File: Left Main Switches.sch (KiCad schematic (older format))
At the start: 80 parts

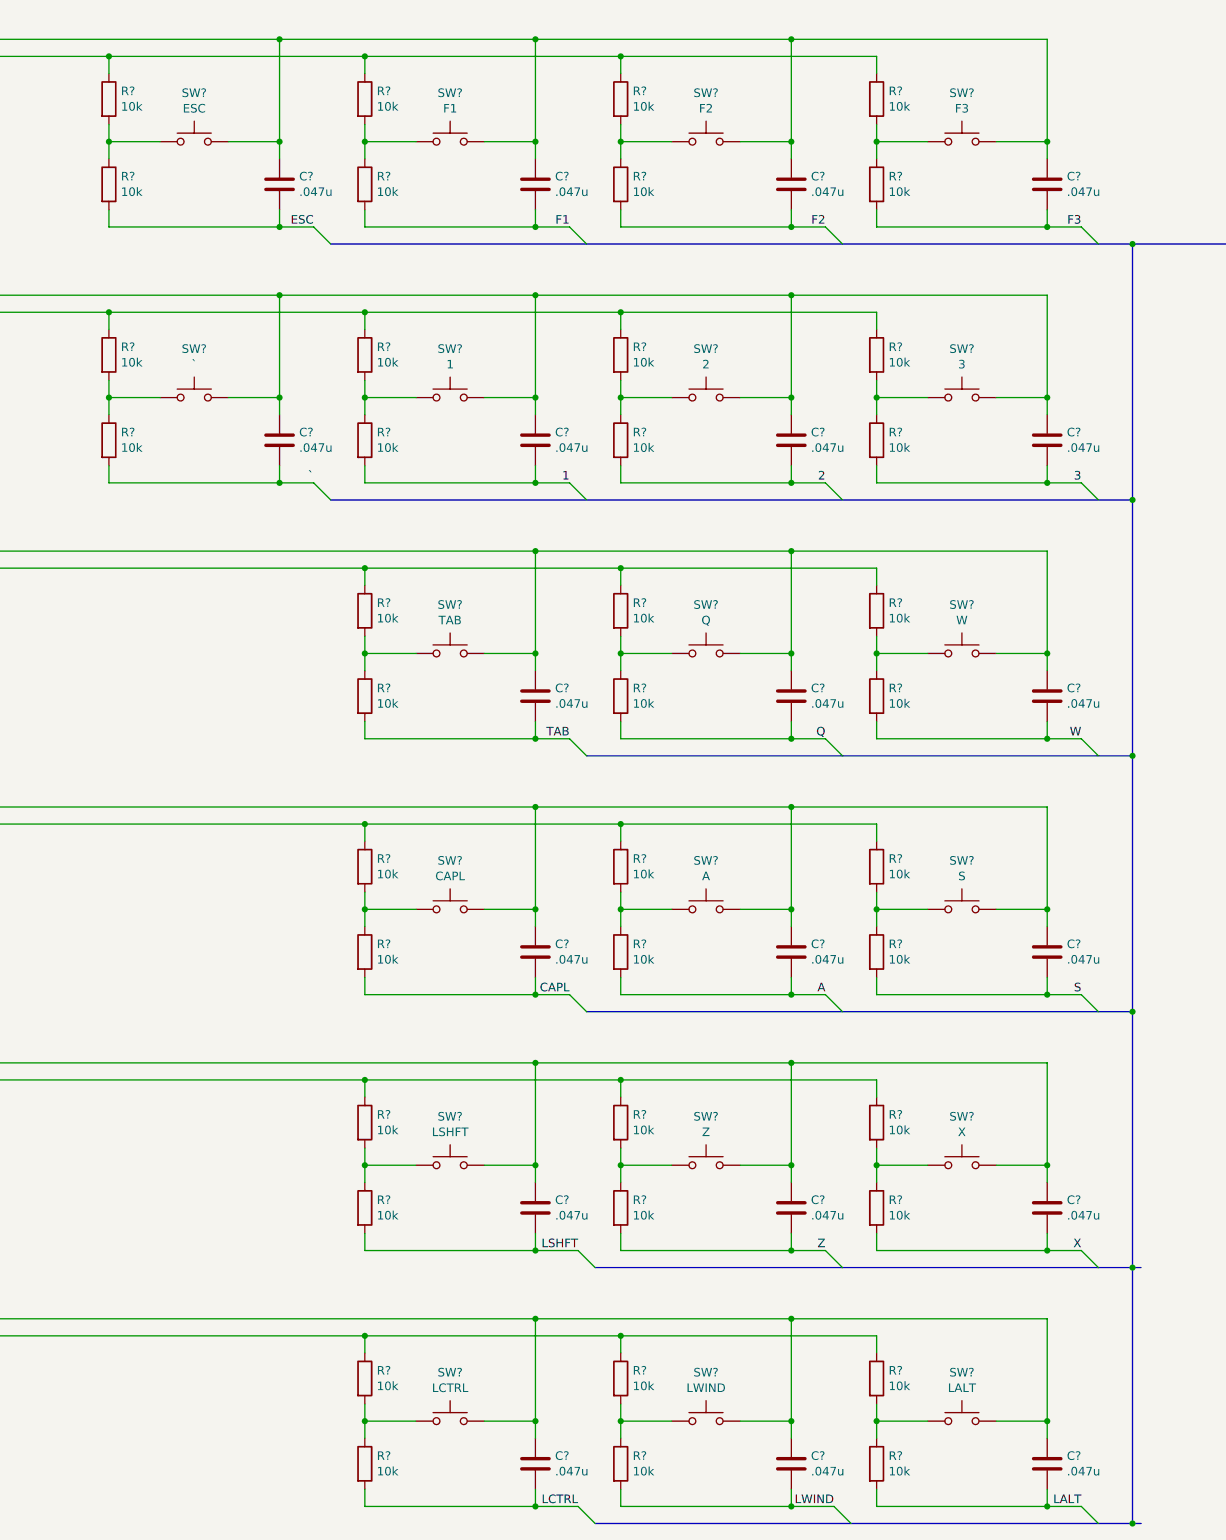
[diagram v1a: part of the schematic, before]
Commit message: Corrected errors found in design rule check
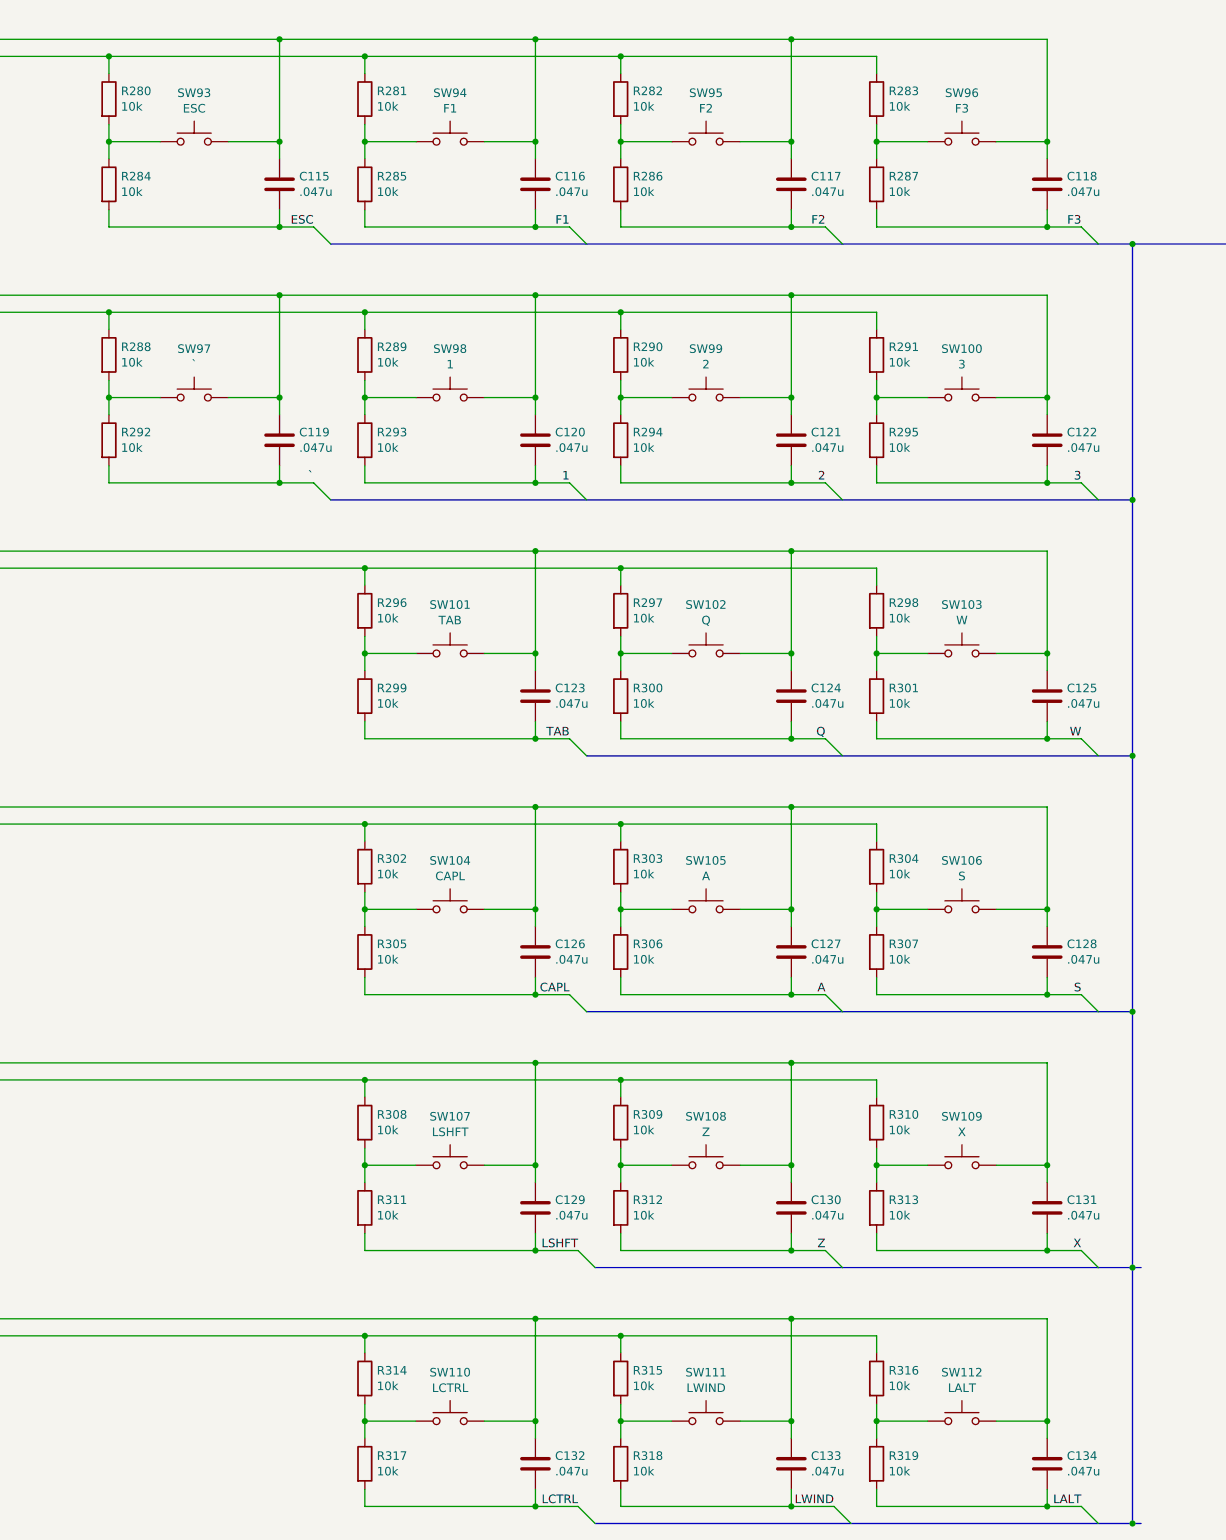
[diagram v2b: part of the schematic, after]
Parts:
- C115, C116, C117, C118, C119, C120, C121, C122, C123, C124, C125, C126, C127, C128, C129, C130, C131, C132, C133, C134: renamed from C?; footprint (none) -> Capacitor_SMD:C_1206_3216Metric_Pad1.42x1.75mm_HandSolder
- R280, R281, R282, R283, R284, R285, R286, R287, R288, R289, R290, R291, R292, R293, R294, R295, R296, R297, R298, R299, R300, R301, R302, R303, R304, R305, R306, R307, R308, R309, R310, R311, R312, R313, R314, R315, R316, R317, R318, R319: renamed from R?; footprint (none) -> Resistor_SMD:R_1206_3216Metric_Pad1.42x1.75mm_HandSolder
- SW100, SW101, SW102, SW103, SW104, SW105, SW106, SW107, SW108, SW109, SW110, SW111, SW112, SW93, SW94, SW95, SW96, SW97, SW98, SW99: renamed from SW?; footprint (none) -> Button_Switch_Keyboard:SW_Cherry_MX_1.00u_PCB

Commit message: Redesigned for single large PCB
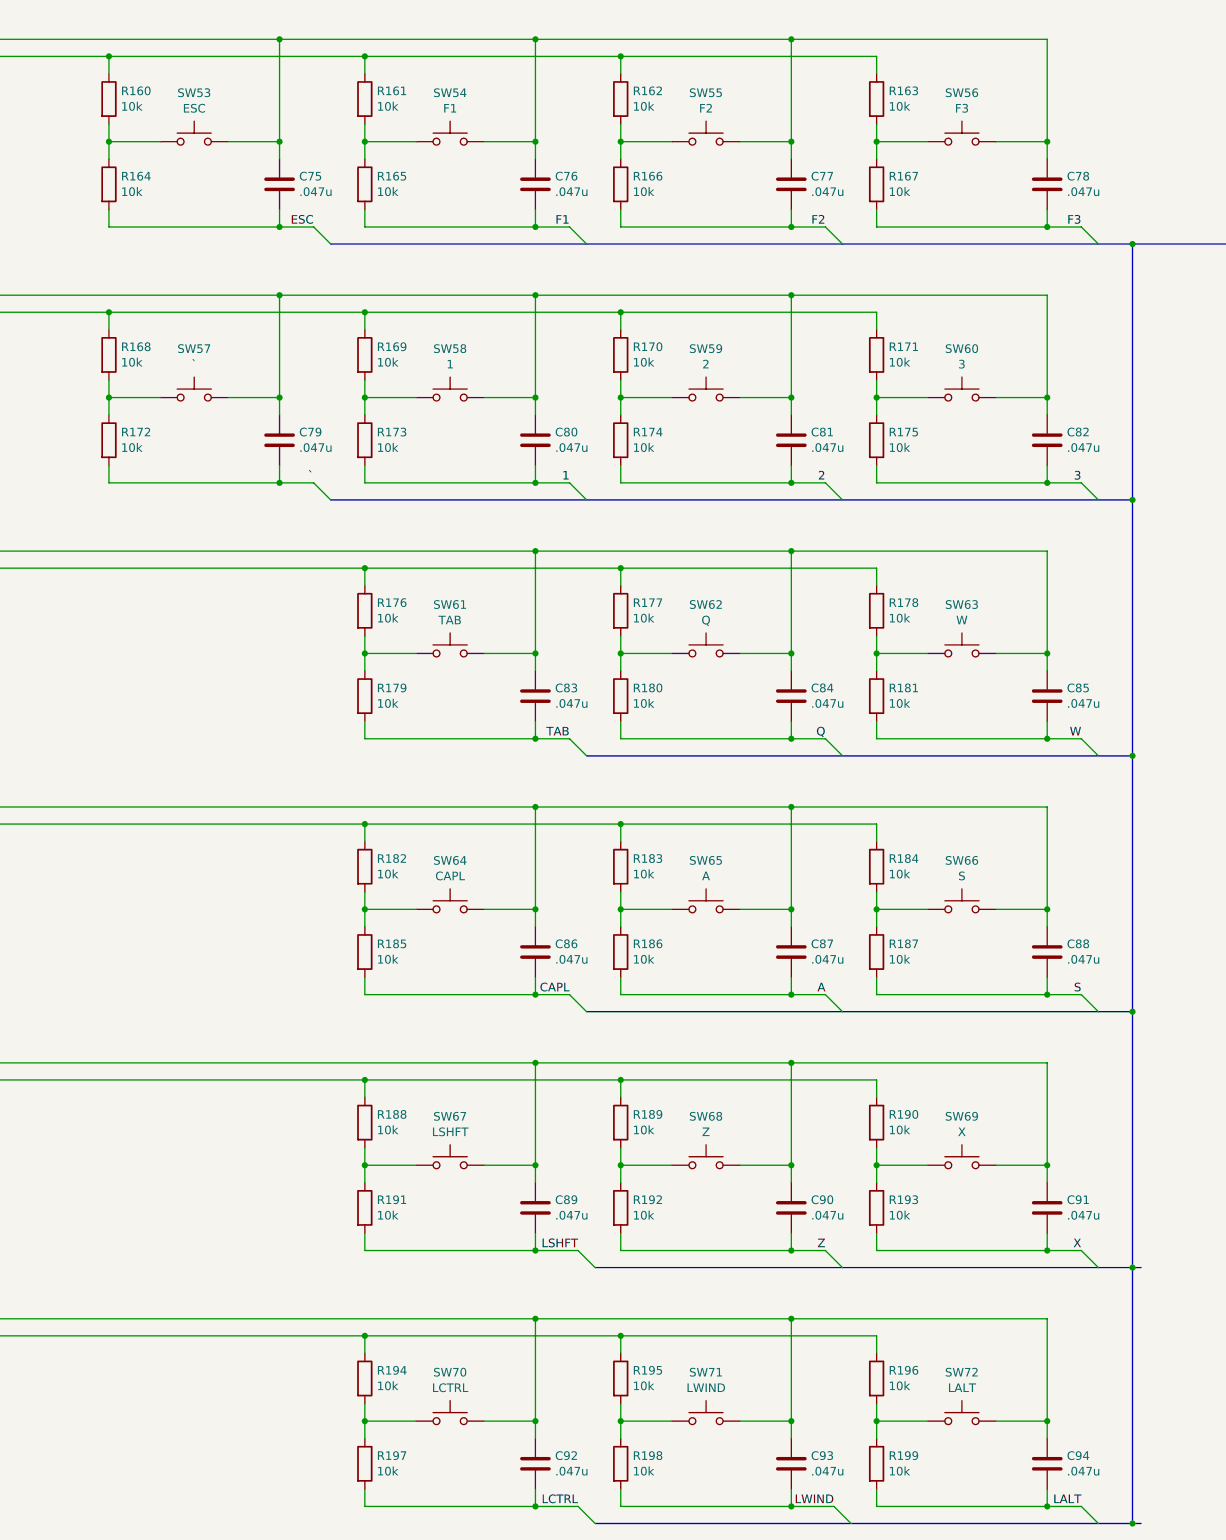
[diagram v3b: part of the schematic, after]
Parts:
- renumbered C115 to C75, C116 to C76, C117 to C77, C118 to C78, C119 to C79, C120 to C80, C121 to C81, C122 to C82, C123 to C83, C124 to C84, C125 to C85, C126 to C86, C127 to C87, C128 to C88, C129 to C89, C130 to C90, C131 to C91, C132 to C92, C133 to C93, C134 to C94, R280 to R160, R281 to R161, R282 to R162, R283 to R163, R284 to R164, R285 to R165, R286 to R166, R287 to R167, R288 to R168, R289 to R169, R290 to R170, R291 to R171, R292 to R172, R293 to R173, R294 to R174, R295 to R175, R296 to R176, R297 to R177, R298 to R178, R299 to R179, R300 to R180, R301 to R181, R302 to R182, R303 to R183, R304 to R184, R305 to R185, R306 to R186, R307 to R187, R308 to R188, R309 to R189, R310 to R190, R311 to R191, R312 to R192, R313 to R193, R314 to R194, R315 to R195, R316 to R196, R317 to R197, R318 to R198, R319 to R199, SW93 to SW53, SW94 to SW54, SW95 to SW55, SW96 to SW56, SW97 to SW57, SW98 to SW58, SW99 to SW59, SW100 to SW60, SW101 to SW61, SW102 to SW62, SW103 to SW63, SW104 to SW64, SW105 to SW65, SW106 to SW66, SW107 to SW67, SW108 to SW68, SW109 to SW69, SW110 to SW70, SW111 to SW71, SW112 to SW72
